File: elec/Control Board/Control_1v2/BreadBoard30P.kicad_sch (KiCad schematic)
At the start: 22 parts, among them J1 Conn_02x06_Odd_Even, J10 Conn_01x30, J11 Conn_01x30, J12 Conn_01x30, J13 Conn_01x30, J14 Conn_01x30, J15 Conn_01x30, J16 Conn_01x30, J17 Conn_01x30, J18 Conn_02x06_Odd_Even, J19 Conn_02x06_Odd_Even, J2 Conn_02x06_Odd_Even, J20 Conn_02x06_Odd_Even, J21 Conn_02x06_Odd_Even, J22 Conn_02x06_Odd_Even, J3 Conn_02x06_Odd_Even, J4 Conn_02x06_Odd_Even, J5 Conn_02x06_Odd_Even, J6 Conn_01x30, J7 Conn_01x30, J8 Conn_01x30, J9 Conn_01x30

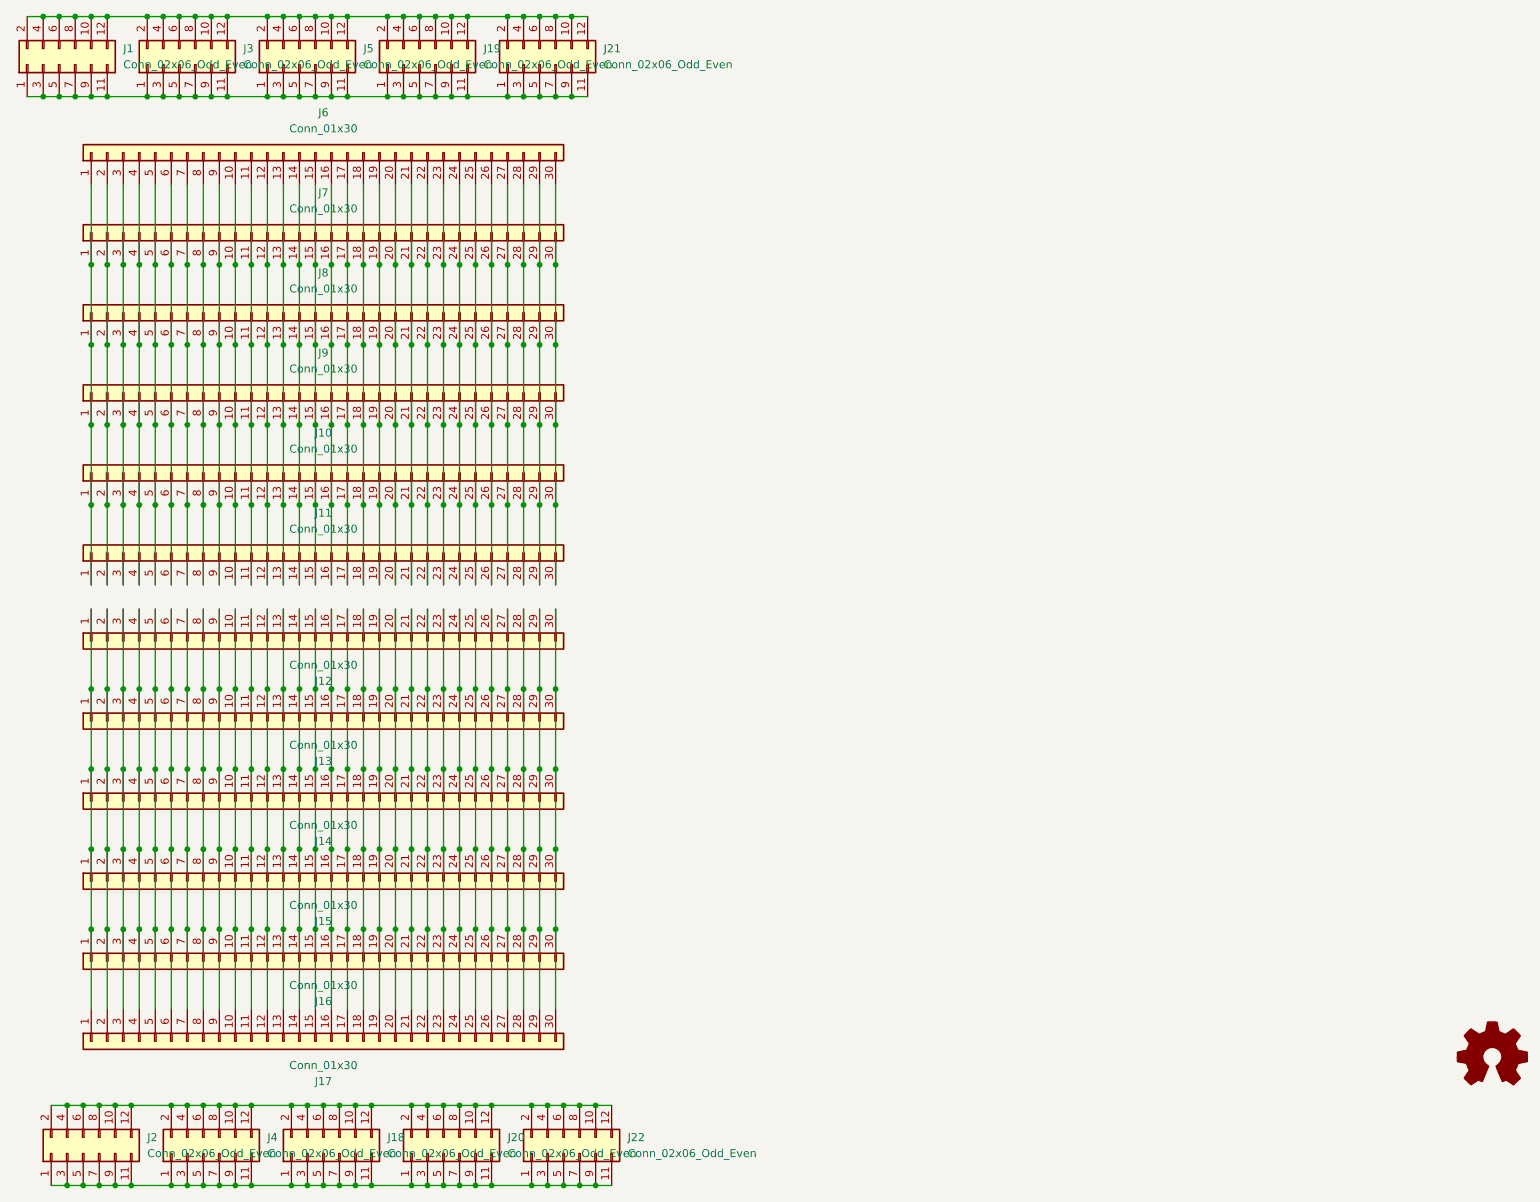
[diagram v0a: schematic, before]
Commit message: PCB V1.2. Add 3d model for power supply footprint. Set many headers connectors for DNI on schematic and PCB.
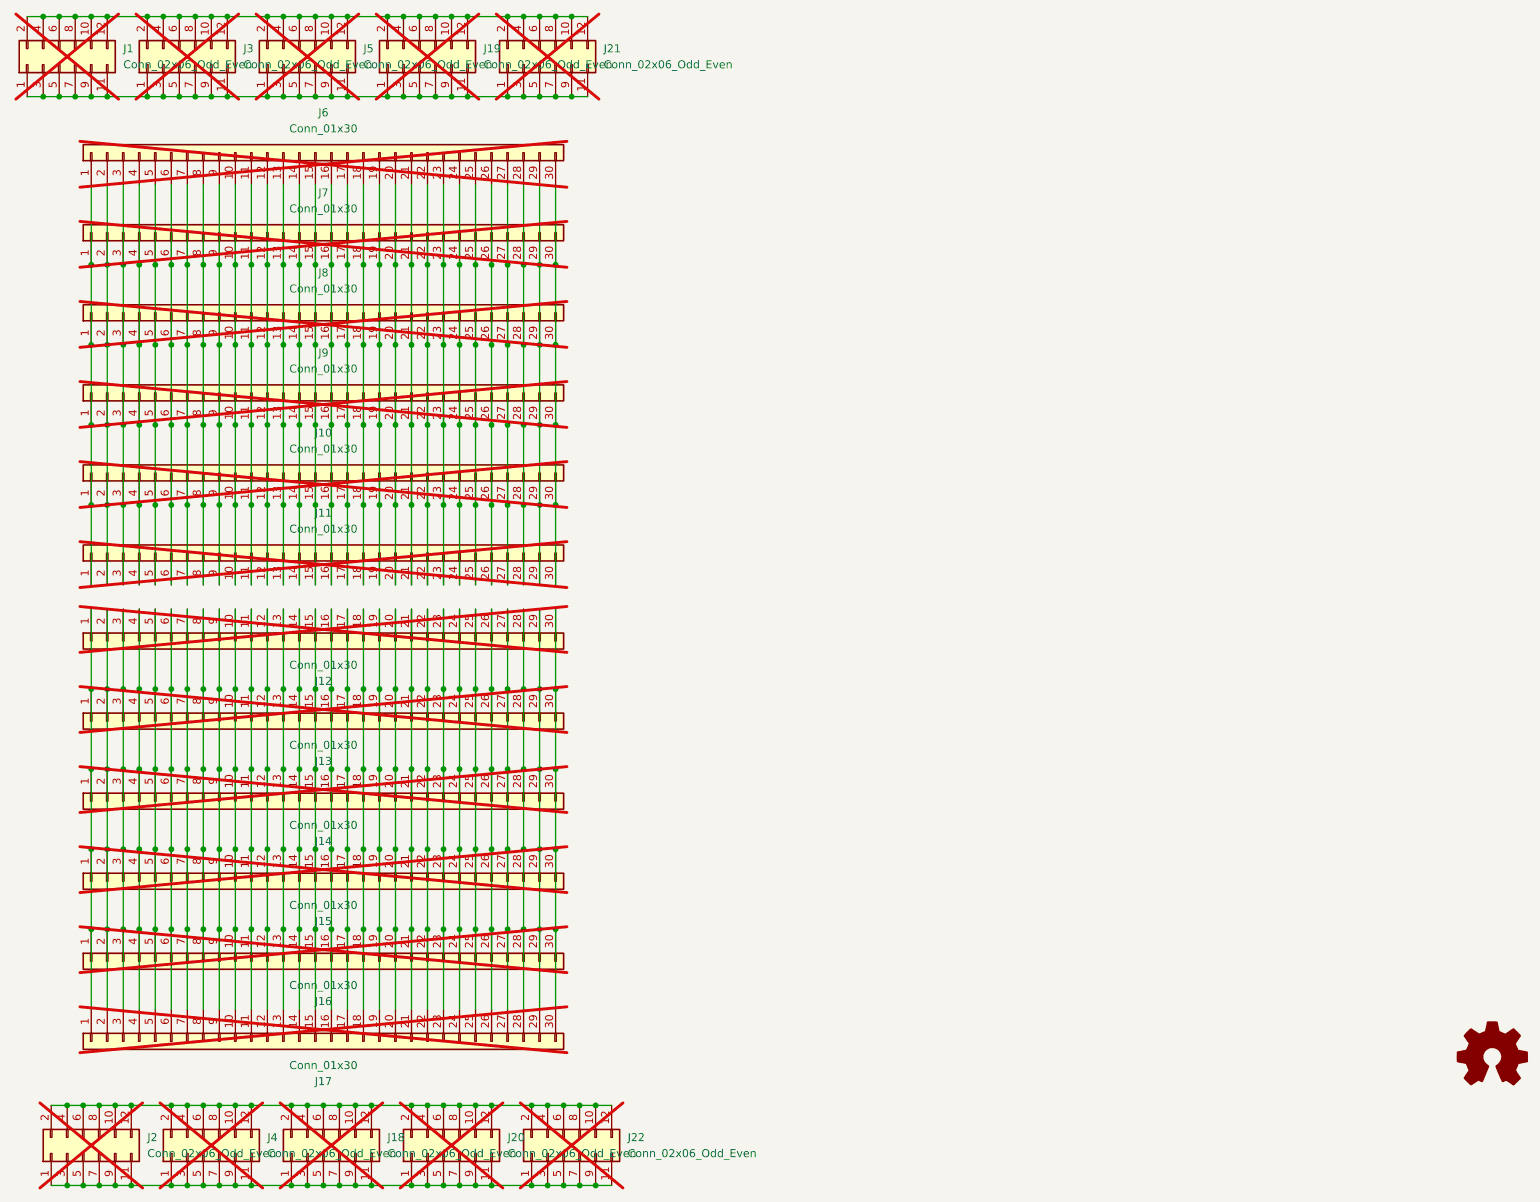
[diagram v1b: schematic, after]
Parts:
- J1, J10, J11, J12, J13, J14, J15, J16, J17, J18, J19, J2, J20, J21, J22, J3, J4, J5, J6, J7, J8, J9: now not fitted; now left out of the parts list
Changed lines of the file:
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@@
   )
   (symbol (lib_id "Connector_Generic:Conn_01x30") (at 77.47 72.39 90) (unit 1)
-    (in_bom yes) (on_board yes) (dnp no) (fields_autoplaced)
+    (in_bom no) (on_board yes) (dnp yes) (fields_autoplaced)
     (property "Reference" "J9" (at 78.74 66.04 90)
       (effects (font (size 1.27 1.27)))
@@
   )
   (symbol (lib_id "Connector_Generic:Conn_01x30") (at 77.47 175.26 90) (mirror x) (unit 1)
-    (in_bom yes) (on_board yes) (dnp no) (fields_autoplaced)
+    (in_bom no) (on_board yes) (dnp yes) (fields_autoplaced)
     (property "Reference" "J17" (at 78.74 181.61 90)
       (effects (font (size 1.27 1.27)))
@@
   )
   (symbol (lib_id "Connector_Generic:Conn_01x30") (at 77.47 85.09 90) (unit 1)
-    (in_bom yes) (on_board yes) (dnp no) (fields_autoplaced)
+    (in_bom no) (on_board yes) (dnp yes) (fields_autoplaced)
     (property "Reference" "J10" (at 78.74 78.74 90)
       (effects (font (size 1.27 1.27)))
@@
   )
   (symbol (lib_id "Connector_Generic:Conn_01x30") (at 77.47 137.16 90) (mirror x) (unit 1)
-    (in_bom yes) (on_board yes) (dnp no) (fields_autoplaced)
+    (in_bom no) (on_board yes) (dnp yes) (fields_autoplaced)
     (property "Reference" "J14" (at 78.74 143.51 90)
       (effects (font (size 1.27 1.27)))
@@
   )
   (symbol (lib_id "Connector_Generic:Conn_02x06_Odd_Even") (at 59.69 193.04 90) (unit 1)
-    (in_bom yes) (on_board yes) (dnp no) (fields_autoplaced)
+    (in_bom no) (on_board yes) (dnp yes) (fields_autoplaced)
     (property "Reference" "J4" (at 69.85 190.5 90)
       (effects (font (size 1.27 1.27)) (justify right))
@@
   )
   (symbol (lib_id "Connector_Generic:Conn_01x30") (at 77.47 149.86 90) (mirror x) (unit 1)
-    (in_bom yes) (on_board yes) (dnp no) (fields_autoplaced)
+    (in_bom no) (on_board yes) (dnp yes) (fields_autoplaced)
     (property "Reference" "J15" (at 78.74 156.21 90)
       (effects (font (size 1.27 1.27)))
@@
   )
   (symbol (lib_id "Connector_Generic:Conn_02x06_Odd_Even") (at 116.84 193.04 90) (unit 1)
-    (in_bom yes) (on_board yes) (dnp no) (fields_autoplaced)
+    (in_bom no) (on_board yes) (dnp yes) (fields_autoplaced)
     (property "Reference" "J22" (at 127 190.5 90)
       (effects (font (size 1.27 1.27)) (justify right))
@@
   )
   (symbol (lib_id "Connector_Generic:Conn_02x06_Odd_Even") (at 36.83 20.32 90) (unit 1)
-    (in_bom yes) (on_board yes) (dnp no) (fields_autoplaced)
+    (in_bom no) (on_board yes) (dnp yes) (fields_autoplaced)
     (property "Reference" "J1" (at 46.99 17.78 90)
       (effects (font (size 1.27 1.27)) (justify right))
@@
   )
   (symbol (lib_id "Connector_Generic:Conn_02x06_Odd_Even") (at 113.03 20.32 90) (unit 1)
-    (in_bom yes) (on_board yes) (dnp no) (fields_autoplaced)
+    (in_bom no) (on_board yes) (dnp yes) (fields_autoplaced)
     (property "Reference" "J21" (at 123.19 17.78 90)
       (effects (font (size 1.27 1.27)) (justify right))
@@
   )
   (symbol (lib_id "Connector_Generic:Conn_02x06_Odd_Even") (at 78.74 193.04 90) (unit 1)
-    (in_bom yes) (on_board yes) (dnp no) (fields_autoplaced)
+    (in_bom no) (on_board yes) (dnp yes) (fields_autoplaced)
     (property "Reference" "J18" (at 88.9 190.5 90)
       (effects (font (size 1.27 1.27)) (justify right))
@@
   )
   (symbol (lib_id "Connector_Generic:Conn_01x30") (at 77.47 111.76 90) (mirror x) (unit 1)
-    (in_bom yes) (on_board yes) (dnp no) (fields_autoplaced)
+    (in_bom no) (on_board yes) (dnp yes) (fields_autoplaced)
     (property "Reference" "J12" (at 78.74 118.11 90)
       (effects (font (size 1.27 1.27)))
@@
   )
   (symbol (lib_id "Connector_Generic:Conn_01x30") (at 77.47 162.56 90) (mirror x) (unit 1)
-    (in_bom yes) (on_board yes) (dnp no) (fields_autoplaced)
+    (in_bom no) (on_board yes) (dnp yes) (fields_autoplaced)
     (property "Reference" "J16" (at 78.74 168.91 90)
       (effects (font (size 1.27 1.27)))
@@
   )
   (symbol (lib_id "Connector_Generic:Conn_01x30") (at 77.47 59.69 90) (unit 1)
-    (in_bom yes) (on_board yes) (dnp no) (fields_autoplaced)
+    (in_bom no) (on_board yes) (dnp yes) (fields_autoplaced)
     (property "Reference" "J8" (at 78.74 53.34 90)
       (effects (font (size 1.27 1.27)))
@@
   )
   (symbol (lib_id "Connector_Generic:Conn_02x06_Odd_Even") (at 55.88 20.32 90) (unit 1)
-    (in_bom yes) (on_board yes) (dnp no) (fields_autoplaced)
+    (in_bom no) (on_board yes) (dnp yes) (fields_autoplaced)
     (property "Reference" "J3" (at 66.04 17.78 90)
       (effects (font (size 1.27 1.27)) (justify right))
@@
   )
   (symbol (lib_id "Connector_Generic:Conn_01x30") (at 77.47 46.99 90) (unit 1)
-    (in_bom yes) (on_board yes) (dnp no) (fields_autoplaced)
+    (in_bom no) (on_board yes) (dnp yes) (fields_autoplaced)
     (property "Reference" "J7" (at 78.74 40.64 90)
       (effects (font (size 1.27 1.27)))
@@
   )
   (symbol (lib_id "Connector_Generic:Conn_01x30") (at 77.47 124.46 90) (mirror x) (unit 1)
-    (in_bom yes) (on_board yes) (dnp no) (fields_autoplaced)
+    (in_bom no) (on_board yes) (dnp yes) (fields_autoplaced)
     (property "Reference" "J13" (at 78.74 130.81 90)
       (effects (font (size 1.27 1.27)))
@@
   )
   (symbol (lib_id "Connector_Generic:Conn_02x06_Odd_Even") (at 93.98 20.32 90) (unit 1)
-    (in_bom yes) (on_board yes) (dnp no) (fields_autoplaced)
+    (in_bom no) (on_board yes) (dnp yes) (fields_autoplaced)
     (property "Reference" "J19" (at 104.14 17.78 90)
       (effects (font (size 1.27 1.27)) (justify right))
@@
   )
   (symbol (lib_id "Connector_Generic:Conn_02x06_Odd_Even") (at 97.79 193.04 90) (unit 1)
-    (in_bom yes) (on_board yes) (dnp no) (fields_autoplaced)
+    (in_bom no) (on_board yes) (dnp yes) (fields_autoplaced)
     (property "Reference" "J20" (at 107.95 190.5 90)
       (effects (font (size 1.27 1.27)) (justify right))
@@
   )
   (symbol (lib_id "Connector_Generic:Conn_01x30") (at 77.47 34.29 90) (unit 1)
-    (in_bom yes) (on_board yes) (dnp no) (fields_autoplaced)
+    (in_bom no) (on_board yes) (dnp yes) (fields_autoplaced)
     (property "Reference" "J6" (at 78.74 27.94 90)
       (effects (font (size 1.27 1.27)))
@@
   )
   (symbol (lib_id "Connector_Generic:Conn_01x30") (at 77.47 97.79 90) (unit 1)
-    (in_bom yes) (on_board yes) (dnp no) (fields_autoplaced)
+    (in_bom no) (on_board yes) (dnp yes) (fields_autoplaced)
     (property "Reference" "J11" (at 78.74 91.44 90)
       (effects (font (size 1.27 1.27)))
@@
   )
   (symbol (lib_id "Connector_Generic:Conn_02x06_Odd_Even") (at 40.64 193.04 90) (unit 1)
-    (in_bom yes) (on_board yes) (dnp no) (fields_autoplaced)
+    (in_bom no) (on_board yes) (dnp yes) (fields_autoplaced)
     (property "Reference" "J2" (at 50.8 190.5 90)
       (effects (font (size 1.27 1.27)) (justify right))
@@
   )
   (symbol (lib_id "Connector_Generic:Conn_02x06_Odd_Even") (at 74.93 20.32 90) (unit 1)
-    (in_bom yes) (on_board yes) (dnp no) (fields_autoplaced)
+    (in_bom no) (on_board yes) (dnp yes) (fields_autoplaced)
     (property "Reference" "J5" (at 85.09 17.78 90)
       (effects (font (size 1.27 1.27)) (justify right))
